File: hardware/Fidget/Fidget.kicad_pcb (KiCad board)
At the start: 2 copper layers, 160 x 100 mm, 92 parts, among them J1 FLASH SPI, J10 ADBUS, J11 SIGBUS, J2 USB_B_Micro, J3 POWER, J4 EXT I/O, J5 SPI2, J6 USART1, J7 I^{2}C1, J8 USART2, J9 ADBUS-EXP, SW1 ~{CRESET}, SW2 UB1, SW3 UB1, U1 AT25SF081-SSHD-X, U10 74ALVC16245DG, U11 74ALVC16245DG, U12 74LVC1G14, U13 74ALVC16245DG, U14 74ALVC16245DG, U15 74AHC16373DG, U16 74AHC16373DG, U17 74LVCC3245APWR, U2 ICE40HX4K-TQ144, U3 AP2112K-3.3, U4 MIC5365-1.2YC5, U5 MIC5365-2.5YC5, U6 KC2520Z16.0000C15XXK, U7 KC3225Z3.68640C1KX00, U8 74ALVC16245DG, U9 74ALVC16245DG

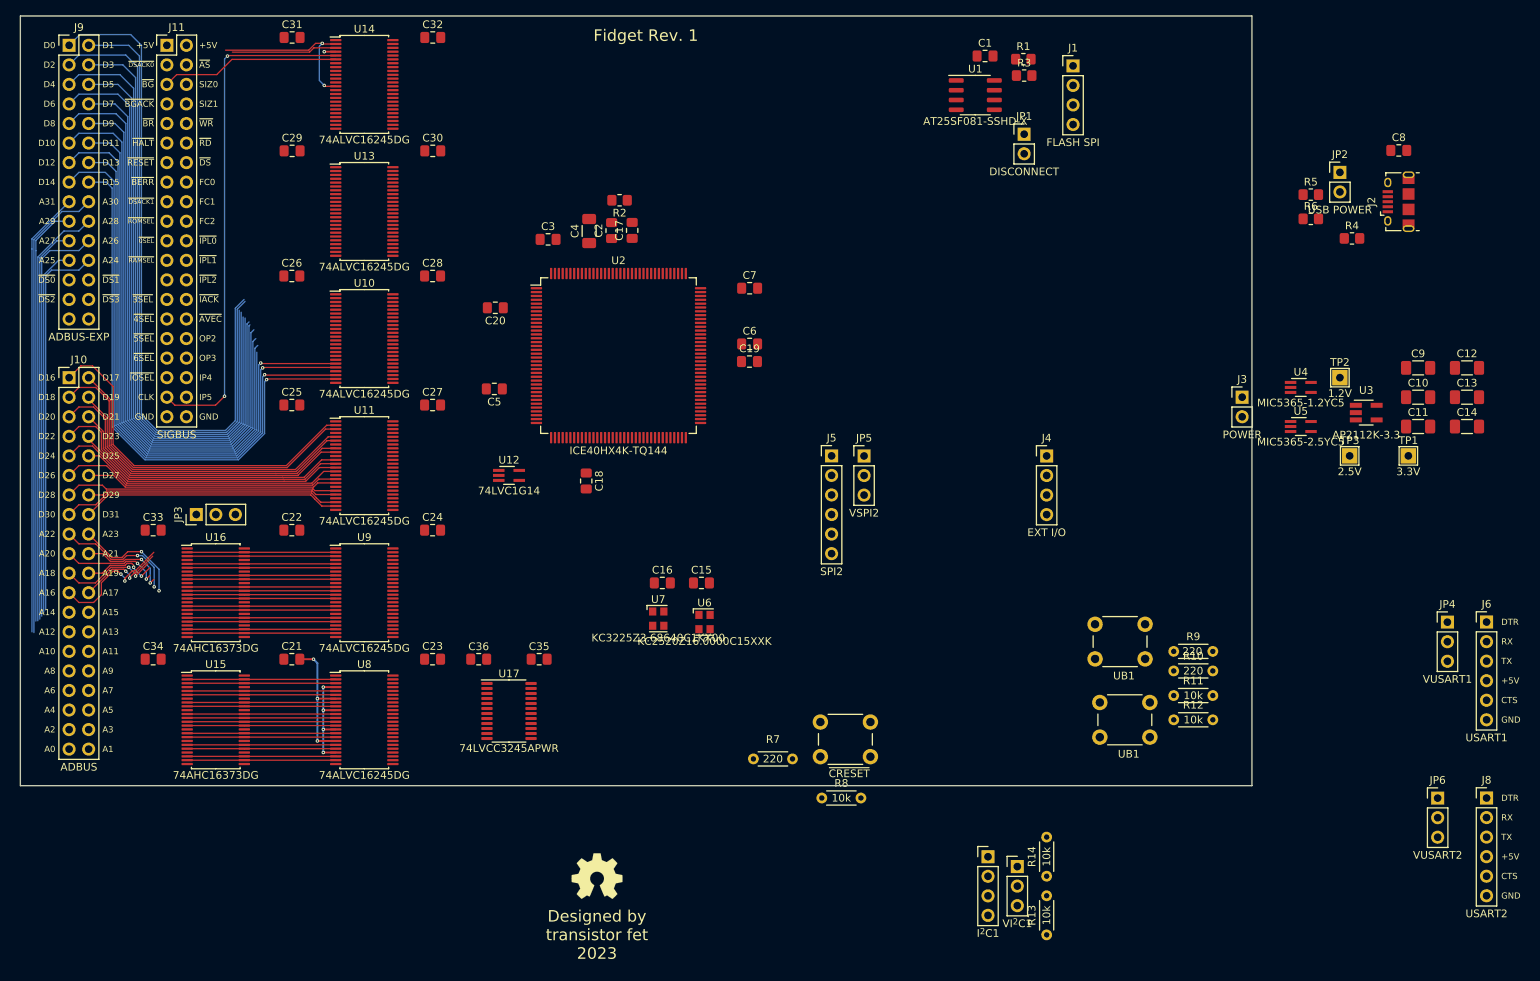
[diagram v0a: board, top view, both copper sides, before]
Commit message: More PCB layout and fixes and reassigments to the schematics
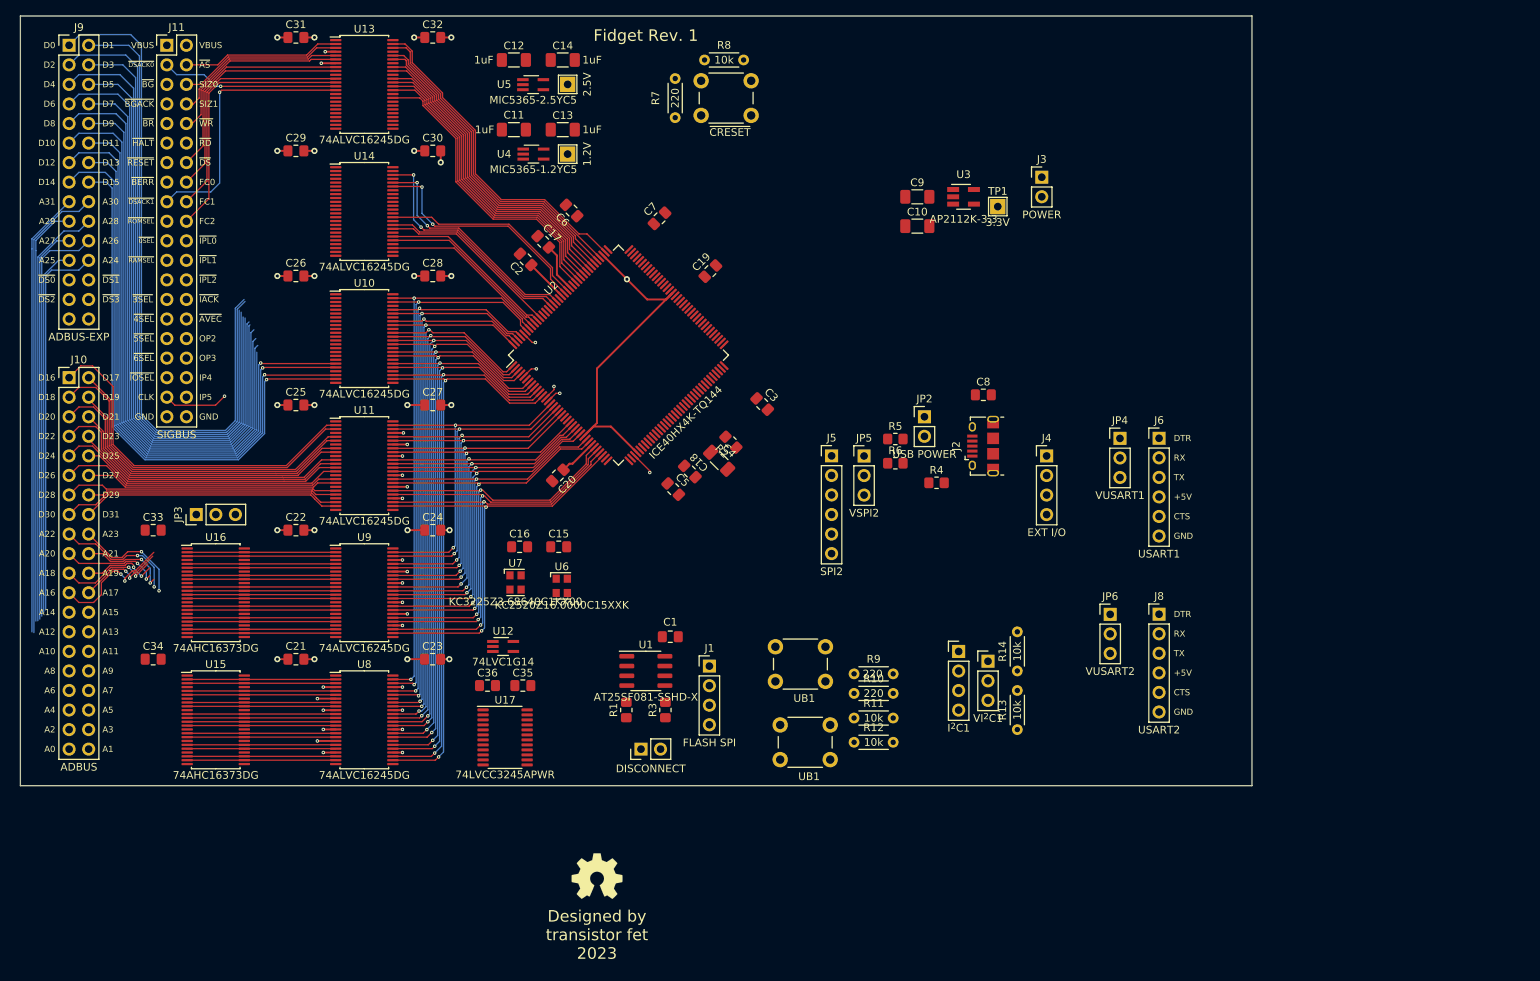
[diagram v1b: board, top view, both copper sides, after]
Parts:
- moved C12 130.1 mm to (107.3, 27.3)
- moved C14 126.8 mm to (113.7, 27.3)
- moved C11 123.6 mm to (107.3, 36.4), turned to 180 degrees
- moved C13 122.5 mm to (113.7, 36.4)
- moved TP3 112.5 mm to (114.3, 30.5)
- moved U5 109.2 mm to (109.8, 30.5)
- moved TP2 104.4 mm to (114.3, 39.5)
- moved U4 104.2 mm to (109.9, 39.5)
- moved R1 99.1 mm to (121.9, 111.8), turned to 90 degrees
- moved R8 97.1 mm to (132.1, 27.3)
- moved R3 94.7 mm to (127.0, 111.8), turned to 90 degrees
- moved JP1 94.1 mm to (123.8, 116.8), turned to 90 degrees
- moved J1 91.2 mm to (132.7, 106.1)
- moved U1 86.2 mm to (124.5, 106.7)
- moved C1 85.8 mm to (127.6, 102.2), turned to 180 degrees
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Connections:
- J11 pad 1: +5V -> VBUS
- J11 pad 2: +5V -> VBUS
- U2 pad 1: USART1_TX -> AD6
- U2 pad 10: USART2_CTS -> AD13
- U2 pad 101: FC0_L -> UL1
- U2 pad 102: FC1_L -> UL2
- U2 pad 104: FC2_L -> UB1
- U2 pad 105: ~{DSACK0_L} -> UB2
- U2 pad 106: ~{DSACK1_L} -> unconnected-(U2-Pad106)
- U2 pad 107: ~{BERR_L} -> unconnected-(U2-Pad107)
- U2 pad 11: SDO2 -> AD14
- U2 pad 110: AD16 -> ~{AS_L}
- U2 pad 112: AD17 -> SIZ0_L
- U2 pad 113: AD18 -> SIZ1_L
- U2 pad 114: AD19 -> R/~{W}_L
- U2 pad 115: AD20 -> ~{DS_L}
- U2 pad 116: AD21 -> FC0_L
- U2 pad 117: AD22 -> FC1_L
- U2 pad 118: AD23 -> FC2_L
- U2 pad 119: ~{HALT_OUT_L} -> ~{DSACK0_L}
- U2 pad 12: SDI2 -> AD15
- U2 pad 120: ~{RESET_OUT_L} -> ~{DSACK1_L}
- U2 pad 121: ~{BG_L} -> ~{BERR_L}
- U2 pad 122: ~{BGACK_L} -> ~{HALT_OUT_L}
- U2 pad 124: ~{BR_L} -> ~{RESET_OUT_L}
- U2 pad 125: ~{AVEC_L} -> ~{BG_L}
- U2 pad 130: AD24 -> ~{BGACK_L}
- U2 pad 134: AD25 -> ~{BR_L}
- U2 pad 135: AD26 -> ~{IPL0_L}
- U2 pad 136: AD27 -> ~{IPL1_L}
- U2 pad 137: AD28 -> ~{IPL2_L}
- U2 pad 138: AD29 -> AD0
- U2 pad 139: AD30 -> AD1
- U2 pad 141: AD31 -> AD2
- U2 pad 142: ~{IPL0_L} -> AD3
- U2 pad 143: ~{IPL1_L} -> AD4
- U2 pad 144: ~{IPL2_L} -> AD5
- U2 pad 15: SCK2 -> AD16
- U2 pad 16: ~{SCS2} -> AD17
- U2 pad 17: SCK1 -> AD18
- U2 pad 18: SDA1 -> AD19
- U2 pad 19: Net-(J4-Pad1) -> AD20
- U2 pad 2: USART1_RX -> AD7
- U2 pad 20: Net-(J4-Pad2) -> ~{HALT_IN_L}
- U2 pad 21: Net-(J4-Pad3) -> ~{IACK_L}
- U2 pad 22: Net-(J4-Pad4) -> AD21
- U2 pad 23: unconnected-(U2-Pad23) -> AD22
- U2 pad 24: unconnected-(U2-Pad24) -> AD23
- U2 pad 25: unconnected-(U2-Pad25) -> AD24
- U2 pad 26: unconnected-(U2-Pad26) -> AD25
- U2 pad 28: unconnected-(U2-Pad28) -> AD26
- U2 pad 29: unconnected-(U2-Pad29) -> AD27
- U2 pad 3: USART1_DTR -> AD8
- U2 pad 31: UL1 -> AD28
- U2 pad 32: UL2 -> AD29
- U2 pad 33: UB1 -> AD30
- U2 pad 34: UB2 -> AD31
- U2 pad 37: USB_PULLUP -> ~{AVEC_L}
- U2 pad 38: USB_DP -> SEND/~{RECV}
- U2 pad 39: USB_DN -> ~{ADDR_OE}
- U2 pad 4: USART1_CTS -> AD9
- U2 pad 41: ~{SF_WP} -> ~{CTRL_OE}
- U2 pad 42: ~{SF_HOLD} -> ~{AL_OE_L}
- U2 pad 43: unconnected-(U2-Pad43) -> ~{AL_LE_L}
- U2 pad 44: unconnected-(U2-Pad44) -> ~{DATA_OE}
- U2 pad 45: SEND/~{RECV} -> ~{DATA_DIR}
- U2 pad 47: ~{ADDR_OE} -> CLK-16M
- U2 pad 48: ~{CTRL_OE} -> CLK-3.6864M
- U2 pad 49: CLK-16M -> ~{ALT_CTRL_OE}
- U2 pad 52: CLK-3.6864M -> ~{ALT_CTRL_DIR1}
- U2 pad 55: ~{AL_OE_L} -> ~{ALT_CTRL_DIR2}
- U2 pad 56: ~{AL_LE_L} -> ~{SF_WP}
- U2 pad 60: ~{DATA_OE} -> ~{SF_HOLD}
- U2 pad 61: ~{DATA_DIR} -> USB_DP
- U2 pad 62: ~{ALT_CTRL_OE} -> USB_DN
- U2 pad 63: ~{ALT_CTRL_DIR1} -> USB_PULLUP
- U2 pad 64: ~{ALT_CTRL_DIR2} -> unconnected-(U2-Pad64)
- U2 pad 7: USART2_TX -> AD10
- U2 pad 73: AD0 -> USART1_TX
- U2 pad 74: AD1 -> USART1_RX
- U2 pad 75: AD2 -> USART1_DTR
- U2 pad 76: AD3 -> USART1_CTS
- U2 pad 78: AD4 -> USART2_TX
- U2 pad 79: AD5 -> USART2_RX
- U2 pad 8: USART2_RX -> AD11
- U2 pad 80: AD6 -> USART2_DTR
- U2 pad 81: AD7 -> USART2_CTS
- U2 pad 82: AD8 -> SDO2
- U2 pad 83: AD9 -> SDI2
- U2 pad 84: AD10 -> SCK2
- U2 pad 85: AD11 -> ~{SCS2}
- U2 pad 87: AD12 -> SCK1
- U2 pad 88: AD13 -> SDA1
- U2 pad 9: USART2_DTR -> AD12
- U2 pad 90: AD14 -> Net-(J4-Pad1)
- U2 pad 91: AD15 -> Net-(J4-Pad2)
- U2 pad 93: ~{HALT_IN_L} -> Net-(J4-Pad3)
- U2 pad 94: ~{IACK_L} -> Net-(J4-Pad4)
- U2 pad 95: ~{AS_L} -> unconnected-(U2-Pad95)
- U2 pad 96: SIZ0_L -> unconnected-(U2-Pad96)
- U2 pad 97: SIZ1_L -> unconnected-(U2-Pad97)
- U2 pad 98: R/~{W}_L -> unconnected-(U2-Pad98)
- U2 pad 99: ~{DS_L} -> unconnected-(U2-Pad99)
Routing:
- net AD15: track 0.00 -> 76.7 mm, vias 0 -> 2
- net AD14: track 0.00 -> 76.1 mm, vias 0 -> 2
- net AD13: track 0.00 -> 75.9 mm, vias 0 -> 2
- net AD12: track 0.00 -> 75.3 mm, vias 0 -> 2
- net AD11: track 0.00 -> 74.9 mm, vias 0 -> 2
- net AD10: track 0.00 -> 74.2 mm, vias 0 -> 2
- net AD9: track 0.00 -> 73.1 mm, vias 0 -> 2
- net AD8: track 0.00 -> 72.6 mm, vias 0 -> 2
- net AD7: track 0.00 -> 72.2 mm, vias 0 -> 2
- net AD6: track 0.00 -> 72.2 mm, vias 0 -> 2
- net AD1: track 0.00 -> 72.1 mm, vias 0 -> 2
- net AD0: track 0.00 -> 71.6 mm, vias 0 -> 2
- net AD2: track 0.00 -> 71.1 mm, vias 0 -> 2
- net AD3: track 0.00 -> 70.9 mm, vias 0 -> 2
- net AD4: track 0.00 -> 70.8 mm, vias 0 -> 2
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- added copper zone on In1.Cu, net +3.3V
- added copper zone on In2.Cu, net GND
- added copper zone on In1.Cu, net VBUS
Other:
- copper layers 2 -> 4
- board text added: "VBUS"
